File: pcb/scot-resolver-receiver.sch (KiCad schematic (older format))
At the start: 12 parts, among them IC3 AD8692ARMZ

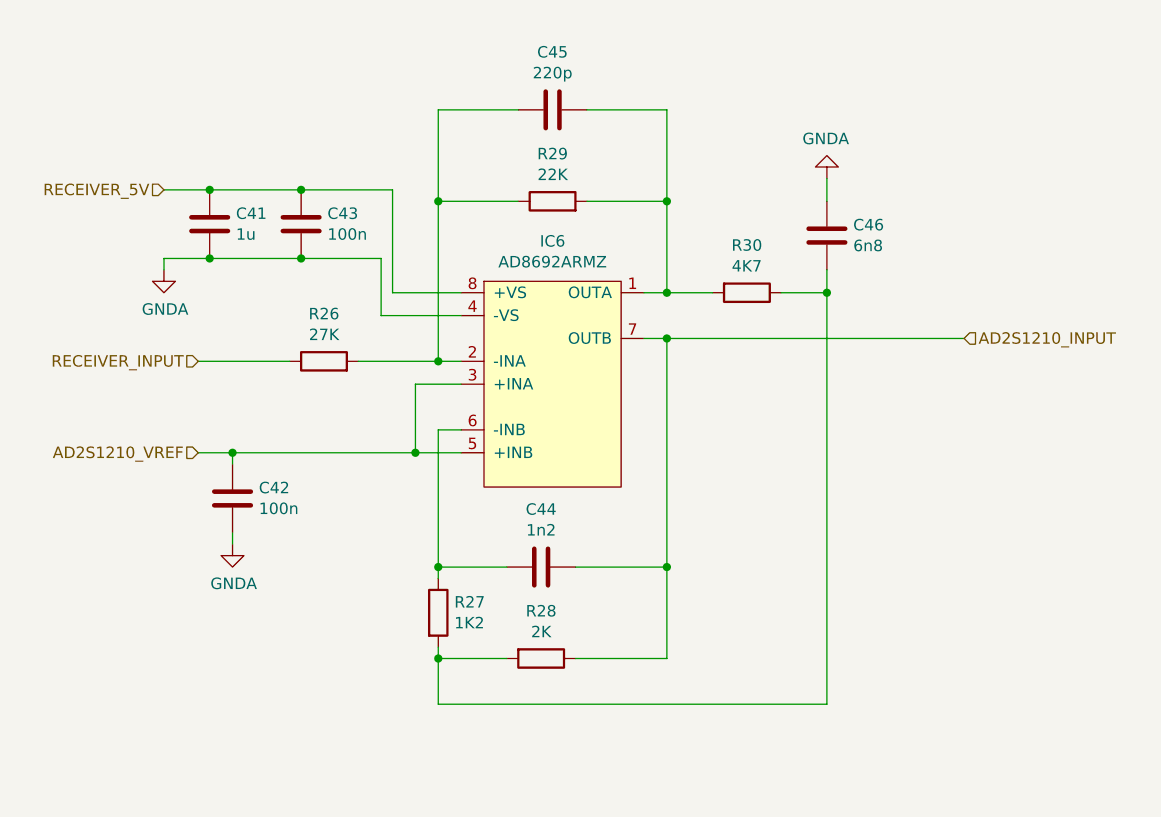
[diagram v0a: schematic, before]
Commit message: PCB Progress, laying tracks.
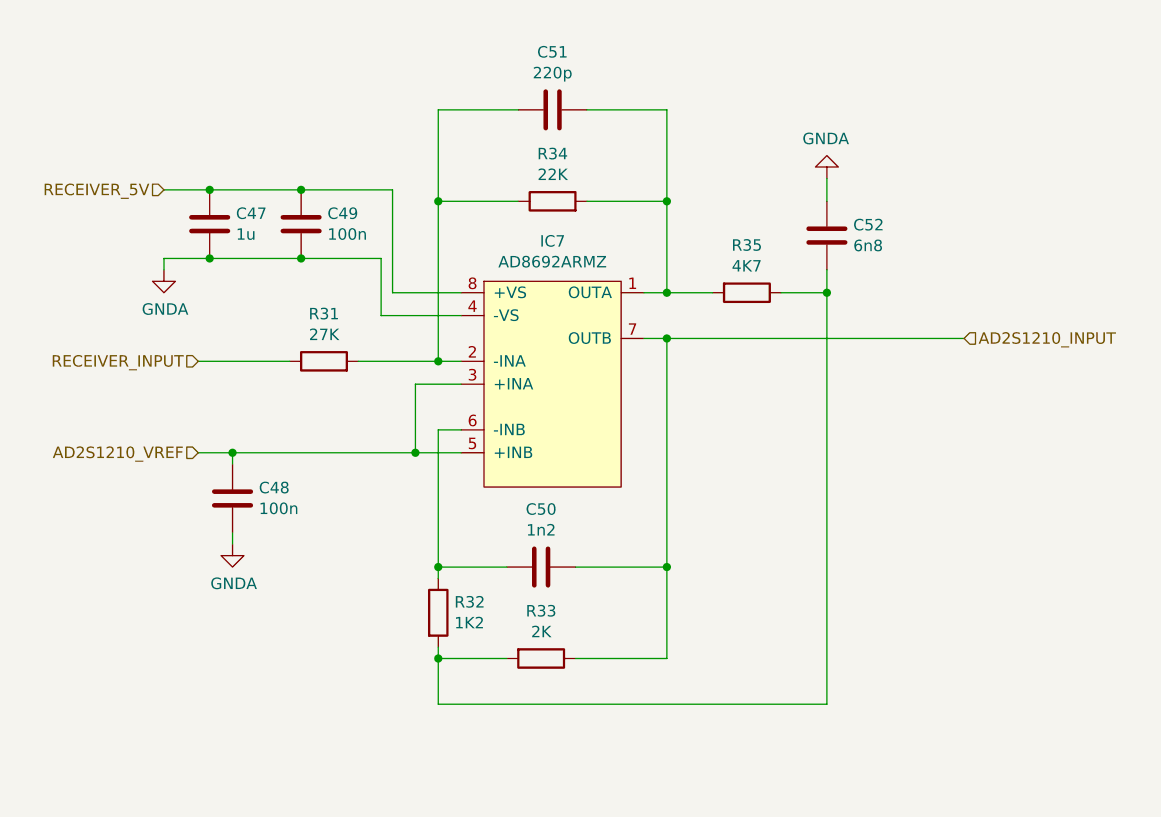
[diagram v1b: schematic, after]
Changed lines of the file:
@@
 $Descr A4 11693 8268
 encoding utf-8
-Sheet 6 9
+Sheet 7 9
 Title ""
 Date ""
@@
 AR Path="/5E46F57D/5E2564F7" Ref="IC6"  Part="1"
 AR Path="/5E46F583/5E2564F7" Ref="IC7"  Part="1"
-F 0 "IC6" H 5100 3925 50  0000 C CNN
+F 0 "IC7" H 5100 3925 50  0000 C CNN
 F 1 "AD8692ARMZ" H 5100 3834 50  0000 C CNN
 F 2 "agg:MSOP-8" H 4800 2700 50  0001 L CNN
@@
 AR Path="/5E46F57D/5E256D1D" Ref="R30"  Part="1"
 AR Path="/5E46F583/5E256D1D" Ref="R35"  Part="1"
-F 0 "R30" V 5743 2900 50  0000 C CNN
+F 0 "R35" V 5743 2900 50  0000 C CNN
 F 1 "4K7" V 5834 2900 50  0000 C CNN
 F 2 "Resistor_SMD:R_0402_1005Metric" V 5880 2900 50  0001 C CNN
@@
 AR Path="/5E46F57D/5E257610" Ref="C46"  Part="1"
 AR Path="/5E46F583/5E257610" Ref="C52"  Part="1"
-F 0 "C46" H 6185 2604 50  0000 R CNN
+F 0 "C52" H 6185 2604 50  0000 R CNN
 F 1 "6n8" H 6185 2695 50  0000 R CNN
 F 2 "Capacitor_SMD:C_0402_1005Metric" H 6338 2500 50  0001 C CNN
@@
 AR Path="/5E46F57D/5E258A95" Ref="R28"  Part="1"
 AR Path="/5E46F583/5E258A95" Ref="R33"  Part="1"
-F 0 "R28" V 4843 4500 50  0000 C CNN
+F 0 "R33" V 4843 4500 50  0000 C CNN
 F 1 "2K" V 4934 4500 50  0000 C CNN
 F 2 "Resistor_SMD:R_0402_1005Metric" V 4980 4500 50  0001 C CNN
@@
 AR Path="/5E46F57D/5E258E42" Ref="C44"  Part="1"
 AR Path="/5E46F583/5E258E42" Ref="C50"  Part="1"
-F 0 "C44" V 5302 4100 50  0000 C CNN
+F 0 "C50" V 5302 4100 50  0000 C CNN
 F 1 "1n2" V 5211 4100 50  0000 C CNN
 F 2 "Capacitor_SMD:C_0402_1005Metric" H 5088 3950 50  0001 C CNN
@@
 AR Path="/5E46F57D/5E25A0BD" Ref="R27"  Part="1"
 AR Path="/5E46F583/5E25A0BD" Ref="R32"  Part="1"
-F 0 "R27" H 4670 4346 50  0000 L CNN
+F 0 "R32" H 4670 4346 50  0000 L CNN
 F 1 "1K2" H 4670 4255 50  0000 L CNN
 F 2 "Resistor_SMD:R_0402_1005Metric" V 4530 4300 50  0001 C CNN
@@
 AR Path="/5E46F57D/5E25CCF3" Ref="R29"  Part="1"
 AR Path="/5E46F583/5E25CCF3" Ref="R34"  Part="1"
-F 0 "R29" V 5307 2500 50  0000 C CNN
+F 0 "R34" V 5307 2500 50  0000 C CNN
 F 1 "22K" V 5216 2500 50  0000 C CNN
 F 2 "Resistor_SMD:R_0402_1005Metric" V 5030 2500 50  0001 C CNN
@@
 AR Path="/5E46F57D/5E25ECB5" Ref="C45"  Part="1"
 AR Path="/5E46F583/5E25ECB5" Ref="C51"  Part="1"
-F 0 "C45" V 5352 2100 50  0000 C CNN
+F 0 "C51" V 5352 2100 50  0000 C CNN
 F 1 "220p" V 5261 2100 50  0000 C CNN
 F 2 "Capacitor_SMD:C_0402_1005Metric" H 5138 1950 50  0001 C CNN
@@
 AR Path="/5E46F57D/5E25FD02" Ref="R26"  Part="1"
 AR Path="/5E46F583/5E25FD02" Ref="R31"  Part="1"
-F 0 "R26" V 4307 3200 50  0000 C CNN
+F 0 "R31" V 4307 3200 50  0000 C CNN
 F 1 "27K" V 4216 3200 50  0000 C CNN
 F 2 "Resistor_SMD:R_0402_1005Metric" V 4030 3200 50  0001 C CNN
@@
 AR Path="/5E46F57D/5E281514" Ref="C43"  Part="1"
 AR Path="/5E46F583/5E281514" Ref="C49"  Part="1"
-F 0 "C43" H 3885 2554 50  0000 R CNN
+F 0 "C49" H 3885 2554 50  0000 R CNN
 F 1 "100n" H 3885 2645 50  0000 R CNN
 F 2 "Capacitor_SMD:C_0402_1005Metric" H 4038 2450 50  0001 C CNN
@@
 AR Path="/5E46F57D/5E297D03" Ref="C42"  Part="1"
 AR Path="/5E46F583/5E297D03" Ref="C48"  Part="1"
-F 0 "C42" H 3585 3754 50  0000 R CNN
+F 0 "C48" H 3585 3754 50  0000 R CNN
 F 1 "100n" H 3585 3845 50  0000 R CNN
 F 2 "Capacitor_SMD:C_0402_1005Metric" H 3738 3650 50  0001 C CNN
@@
 AR Path="/5E46F57D/5E29C4B1" Ref="C41"  Part="1"
 AR Path="/5E46F583/5E29C4B1" Ref="C47"  Part="1"
-F 0 "C41" H 3485 2554 50  0000 R CNN
+F 0 "C47" H 3485 2554 50  0000 R CNN
 F 1 "1u" H 3485 2645 50  0000 R CNN
 F 2 "Capacitor_SMD:C_0603_1608Metric_Pad1.05x0.95mm_HandSolder" H 3638 2450 50  0001 C CNN
@@
 AR Path="/5E46F57D/5E28F597" Ref="#PWR0130"  Part="1"
 AR Path="/5E46F583/5E28F597" Ref="#PWR0133"  Part="1"
-F 0 "#PWR0130" H 3400 2550 50  0001 C CNN
+F 0 "#PWR0133" H 3400 2550 50  0001 C CNN
 F 1 "GNDA" H 3405 2627 50  0000 C CNN
 F 2 "" H 3400 2800 50  0001 C CNN
@@
 AR Path="/5E46F57D/5E28F9AD" Ref="#PWR0131"  Part="1"
 AR Path="/5E46F583/5E28F9AD" Ref="#PWR0134"  Part="1"
-F 0 "#PWR0131" H 3700 3750 50  0001 C CNN
+F 0 "#PWR0134" H 3700 3750 50  0001 C CNN
 F 1 "GNDA" H 3705 3827 50  0000 C CNN
 F 2 "" H 3700 4000 50  0001 C CNN
@@
 AR Path="/5E46F57D/5E28FD4C" Ref="#PWR0132"  Part="1"
 AR Path="/5E46F583/5E28FD4C" Ref="#PWR0135"  Part="1"
-F 0 "#PWR0132" H 6300 2150 50  0001 C CNN
+F 0 "#PWR0135" H 6300 2150 50  0001 C CNN
 F 1 "GNDA" H 6305 2227 50  0000 C CNN
 F 2 "" H 6300 2400 50  0001 C CNN

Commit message: pcb: V2 schematic updates (PCB still to do).
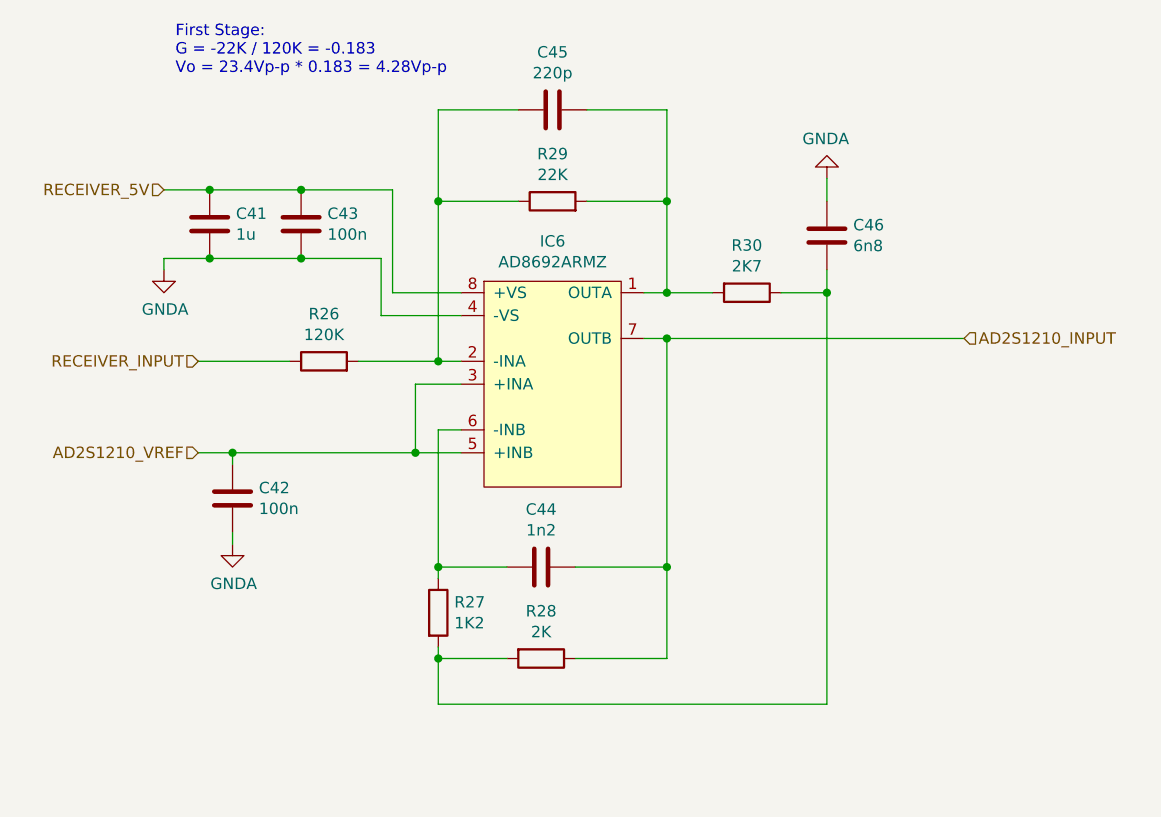
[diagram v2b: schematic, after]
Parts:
- R13: value 27K -> 120K
- R17: value 4K7 -> 2K7
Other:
- note added: "First Stage:\nG = -22K / 120K = -0.183\nVo = 23.4Vp-p * 0.183 = 4.28Vp-p"
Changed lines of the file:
@@
 $Descr A4 11693 8268
 encoding utf-8
-Sheet 7 9
+Sheet 5 7
 Title ""
 Date ""
@@
 AR Path="/5E46F57D/5E2564F7" Ref="IC6"  Part="1"
 AR Path="/5E46F583/5E2564F7" Ref="IC7"  Part="1"
-F 0 "IC7" H 5100 3925 50  0000 C CNN
+F 0 "IC6" H 5100 3925 50  0000 C CNN
 F 1 "AD8692ARMZ" H 5100 3834 50  0000 C CNN
 F 2 "agg:MSOP-8" H 4800 2700 50  0001 L CNN
@@
 AR Path="/5E46F57D/5E256D1D" Ref="R30"  Part="1"
 AR Path="/5E46F583/5E256D1D" Ref="R35"  Part="1"
-F 0 "R35" V 5743 2900 50  0000 C CNN
-F 1 "4K7" V 5834 2900 50  0000 C CNN
+F 0 "R30" V 5743 2900 50  0000 C CNN
+F 1 "2K7" V 5834 2900 50  0000 C CNN
 F 2 "Resistor_SMD:R_0402_1005Metric" V 5880 2900 50  0001 C CNN
 F 3 "~" H 5950 2900 50  0001 C CNN
@@
 AR Path="/5E46F57D/5E257610" Ref="C46"  Part="1"
 AR Path="/5E46F583/5E257610" Ref="C52"  Part="1"
-F 0 "C52" H 6185 2604 50  0000 R CNN
+F 0 "C46" H 6185 2604 50  0000 R CNN
 F 1 "6n8" H 6185 2695 50  0000 R CNN
 F 2 "Capacitor_SMD:C_0402_1005Metric" H 6338 2500 50  0001 C CNN
@@
 AR Path="/5E46F57D/5E258A95" Ref="R28"  Part="1"
 AR Path="/5E46F583/5E258A95" Ref="R33"  Part="1"
-F 0 "R33" V 4843 4500 50  0000 C CNN
+F 0 "R28" V 4843 4500 50  0000 C CNN
 F 1 "2K" V 4934 4500 50  0000 C CNN
 F 2 "Resistor_SMD:R_0402_1005Metric" V 4980 4500 50  0001 C CNN
@@
 AR Path="/5E46F57D/5E258E42" Ref="C44"  Part="1"
 AR Path="/5E46F583/5E258E42" Ref="C50"  Part="1"
-F 0 "C50" V 5302 4100 50  0000 C CNN
+F 0 "C44" V 5302 4100 50  0000 C CNN
 F 1 "1n2" V 5211 4100 50  0000 C CNN
 F 2 "Capacitor_SMD:C_0402_1005Metric" H 5088 3950 50  0001 C CNN
@@
 AR Path="/5E46F57D/5E25A0BD" Ref="R27"  Part="1"
 AR Path="/5E46F583/5E25A0BD" Ref="R32"  Part="1"
-F 0 "R32" H 4670 4346 50  0000 L CNN
+F 0 "R27" H 4670 4346 50  0000 L CNN
 F 1 "1K2" H 4670 4255 50  0000 L CNN
 F 2 "Resistor_SMD:R_0402_1005Metric" V 4530 4300 50  0001 C CNN
@@
 AR Path="/5E46F57D/5E25CCF3" Ref="R29"  Part="1"
 AR Path="/5E46F583/5E25CCF3" Ref="R34"  Part="1"
-F 0 "R34" V 5307 2500 50  0000 C CNN
+F 0 "R29" V 5307 2500 50  0000 C CNN
 F 1 "22K" V 5216 2500 50  0000 C CNN
 F 2 "Resistor_SMD:R_0402_1005Metric" V 5030 2500 50  0001 C CNN
@@
 AR Path="/5E46F57D/5E25ECB5" Ref="C45"  Part="1"
 AR Path="/5E46F583/5E25ECB5" Ref="C51"  Part="1"
-F 0 "C51" V 5352 2100 50  0000 C CNN
+F 0 "C45" V 5352 2100 50  0000 C CNN
 F 1 "220p" V 5261 2100 50  0000 C CNN
 F 2 "Capacitor_SMD:C_0402_1005Metric" H 5138 1950 50  0001 C CNN
@@
 AR Path="/5E46F57D/5E25FD02" Ref="R26"  Part="1"
 AR Path="/5E46F583/5E25FD02" Ref="R31"  Part="1"
-F 0 "R31" V 4307 3200 50  0000 C CNN
-F 1 "27K" V 4216 3200 50  0000 C CNN
+F 0 "R26" V 4307 3200 50  0000 C CNN
+F 1 "120K" V 4216 3200 50  0000 C CNN
 F 2 "Resistor_SMD:R_0402_1005Metric" V 4030 3200 50  0001 C CNN
 F 3 "~" H 4100 3200 50  0001 C CNN
@@
 AR Path="/5E46F57D/5E281514" Ref="C43"  Part="1"
 AR Path="/5E46F583/5E281514" Ref="C49"  Part="1"
-F 0 "C49" H 3885 2554 50  0000 R CNN
+F 0 "C43" H 3885 2554 50  0000 R CNN
 F 1 "100n" H 3885 2645 50  0000 R CNN
 F 2 "Capacitor_SMD:C_0402_1005Metric" H 4038 2450 50  0001 C CNN
@@
 AR Path="/5E46F57D/5E297D03" Ref="C42"  Part="1"
 AR Path="/5E46F583/5E297D03" Ref="C48"  Part="1"
-F 0 "C48" H 3585 3754 50  0000 R CNN
+F 0 "C42" H 3585 3754 50  0000 R CNN
 F 1 "100n" H 3585 3845 50  0000 R CNN
 F 2 "Capacitor_SMD:C_0402_1005Metric" H 3738 3650 50  0001 C CNN
@@
 AR Path="/5E46F57D/5E29C4B1" Ref="C41"  Part="1"
 AR Path="/5E46F583/5E29C4B1" Ref="C47"  Part="1"
-F 0 "C47" H 3485 2554 50  0000 R CNN
+F 0 "C41" H 3485 2554 50  0000 R CNN
 F 1 "1u" H 3485 2645 50  0000 R CNN
 F 2 "Capacitor_SMD:C_0603_1608Metric_Pad1.05x0.95mm_HandSolder" H 3638 2450 50  0001 C CNN
@@
 AR Path="/5E46F57D/5E28F597" Ref="#PWR0130"  Part="1"
 AR Path="/5E46F583/5E28F597" Ref="#PWR0133"  Part="1"
-F 0 "#PWR0133" H 3400 2550 50  0001 C CNN
+F 0 "#PWR0130" H 3400 2550 50  0001 C CNN
 F 1 "GNDA" H 3405 2627 50  0000 C CNN
 F 2 "" H 3400 2800 50  0001 C CNN
@@
 AR Path="/5E46F57D/5E28F9AD" Ref="#PWR0131"  Part="1"
 AR Path="/5E46F583/5E28F9AD" Ref="#PWR0134"  Part="1"
-F 0 "#PWR0134" H 3700 3750 50  0001 C CNN
+F 0 "#PWR0131" H 3700 3750 50  0001 C CNN
 F 1 "GNDA" H 3705 3827 50  0000 C CNN
 F 2 "" H 3700 4000 50  0001 C CNN
@@
 AR Path="/5E46F57D/5E28FD4C" Ref="#PWR0132"  Part="1"
 AR Path="/5E46F583/5E28FD4C" Ref="#PWR0135"  Part="1"
-F 0 "#PWR0135" H 6300 2150 50  0001 C CNN
+F 0 "#PWR0132" H 6300 2150 50  0001 C CNN
 F 1 "GNDA" H 6305 2227 50  0000 C CNN
 F 2 "" H 6300 2400 50  0001 C CNN
@@
 	-1   0    0    1
 $EndComp
+Text Notes 3450 1950 0    50   ~ 0
+First Stage:\nG = -22K / 120K = -0.183\nVo = 23.4Vp-p * 0.183 = 4.28Vp-p
 $EndSCHEMATC

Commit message: pcb: Add Receiver second stage calculations to schematic.
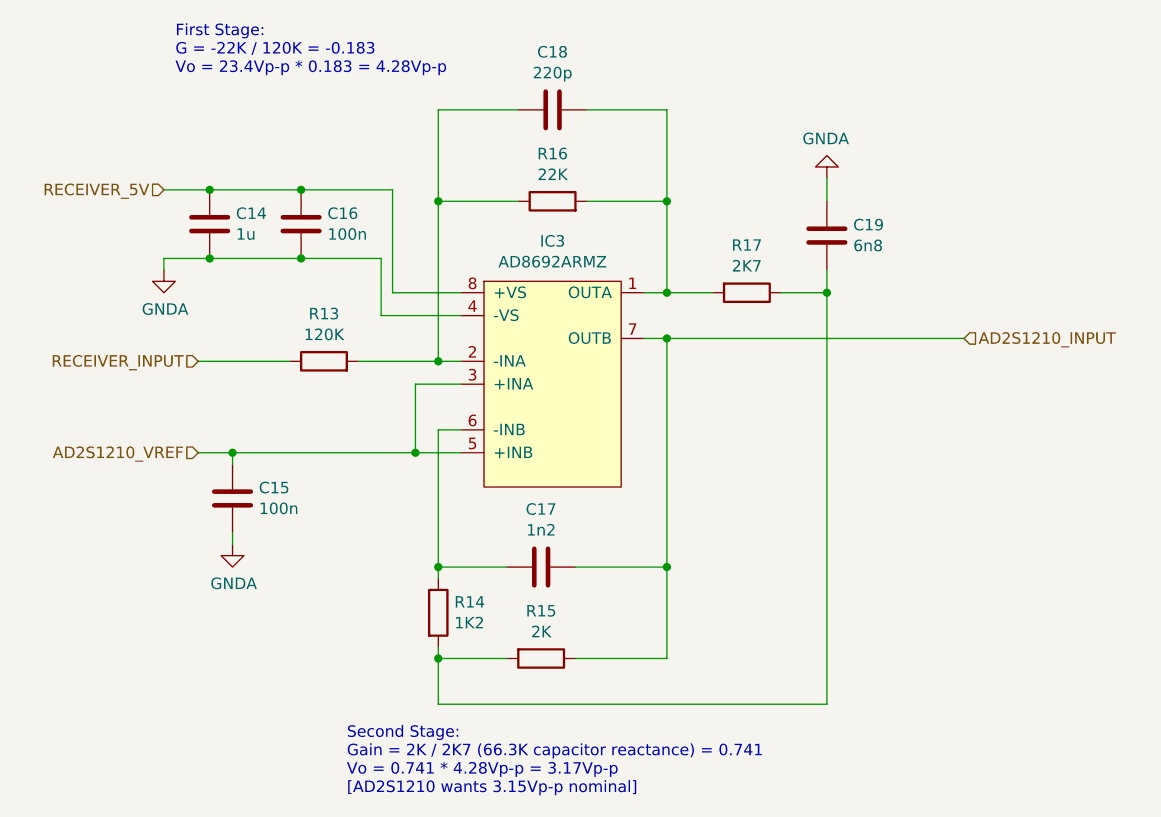
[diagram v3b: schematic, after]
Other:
- note added: "Second Stage:\nGain = 2K / 2K7 (66.3K capacitor reactance) = 0.741\nVo = 0.741 * 4.28Vp-p = 3.17Vp-p\n[AD2S1210 wants 3.15Vp-p nominal]"
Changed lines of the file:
@@
 $Descr A4 11693 8268
 encoding utf-8
-Sheet 5 7
+Sheet 3 7
 Title ""
 Date ""
@@
 AR Path="/5E46F57D/5E2564F7" Ref="IC6"  Part="1"
 AR Path="/5E46F583/5E2564F7" Ref="IC7"  Part="1"
-F 0 "IC6" H 5100 3925 50  0000 C CNN
+F 0 "IC3" H 5100 3925 50  0000 C CNN
 F 1 "AD8692ARMZ" H 5100 3834 50  0000 C CNN
 F 2 "agg:MSOP-8" H 4800 2700 50  0001 L CNN
@@
 AR Path="/5E46F57D/5E256D1D" Ref="R30"  Part="1"
 AR Path="/5E46F583/5E256D1D" Ref="R35"  Part="1"
-F 0 "R30" V 5743 2900 50  0000 C CNN
+F 0 "R17" V 5743 2900 50  0000 C CNN
 F 1 "2K7" V 5834 2900 50  0000 C CNN
 F 2 "Resistor_SMD:R_0402_1005Metric" V 5880 2900 50  0001 C CNN
@@
 AR Path="/5E46F57D/5E257610" Ref="C46"  Part="1"
 AR Path="/5E46F583/5E257610" Ref="C52"  Part="1"
-F 0 "C46" H 6185 2604 50  0000 R CNN
+F 0 "C19" H 6185 2604 50  0000 R CNN
 F 1 "6n8" H 6185 2695 50  0000 R CNN
 F 2 "Capacitor_SMD:C_0402_1005Metric" H 6338 2500 50  0001 C CNN
@@
 AR Path="/5E46F57D/5E258A95" Ref="R28"  Part="1"
 AR Path="/5E46F583/5E258A95" Ref="R33"  Part="1"
-F 0 "R28" V 4843 4500 50  0000 C CNN
+F 0 "R15" V 4843 4500 50  0000 C CNN
 F 1 "2K" V 4934 4500 50  0000 C CNN
 F 2 "Resistor_SMD:R_0402_1005Metric" V 4980 4500 50  0001 C CNN
@@
 AR Path="/5E46F57D/5E258E42" Ref="C44"  Part="1"
 AR Path="/5E46F583/5E258E42" Ref="C50"  Part="1"
-F 0 "C44" V 5302 4100 50  0000 C CNN
+F 0 "C17" V 5302 4100 50  0000 C CNN
 F 1 "1n2" V 5211 4100 50  0000 C CNN
 F 2 "Capacitor_SMD:C_0402_1005Metric" H 5088 3950 50  0001 C CNN
@@
 AR Path="/5E46F57D/5E25A0BD" Ref="R27"  Part="1"
 AR Path="/5E46F583/5E25A0BD" Ref="R32"  Part="1"
-F 0 "R27" H 4670 4346 50  0000 L CNN
+F 0 "R14" H 4670 4346 50  0000 L CNN
 F 1 "1K2" H 4670 4255 50  0000 L CNN
 F 2 "Resistor_SMD:R_0402_1005Metric" V 4530 4300 50  0001 C CNN
@@
 AR Path="/5E46F57D/5E25CCF3" Ref="R29"  Part="1"
 AR Path="/5E46F583/5E25CCF3" Ref="R34"  Part="1"
-F 0 "R29" V 5307 2500 50  0000 C CNN
+F 0 "R16" V 5307 2500 50  0000 C CNN
 F 1 "22K" V 5216 2500 50  0000 C CNN
 F 2 "Resistor_SMD:R_0402_1005Metric" V 5030 2500 50  0001 C CNN
@@
 AR Path="/5E46F57D/5E25ECB5" Ref="C45"  Part="1"
 AR Path="/5E46F583/5E25ECB5" Ref="C51"  Part="1"
-F 0 "C45" V 5352 2100 50  0000 C CNN
+F 0 "C18" V 5352 2100 50  0000 C CNN
 F 1 "220p" V 5261 2100 50  0000 C CNN
 F 2 "Capacitor_SMD:C_0402_1005Metric" H 5138 1950 50  0001 C CNN
@@
 AR Path="/5E46F57D/5E25FD02" Ref="R26"  Part="1"
 AR Path="/5E46F583/5E25FD02" Ref="R31"  Part="1"
-F 0 "R26" V 4307 3200 50  0000 C CNN
+F 0 "R13" V 4307 3200 50  0000 C CNN
 F 1 "120K" V 4216 3200 50  0000 C CNN
 F 2 "Resistor_SMD:R_0402_1005Metric" V 4030 3200 50  0001 C CNN
@@
 AR Path="/5E46F57D/5E281514" Ref="C43"  Part="1"
 AR Path="/5E46F583/5E281514" Ref="C49"  Part="1"
-F 0 "C43" H 3885 2554 50  0000 R CNN
+F 0 "C16" H 3885 2554 50  0000 R CNN
 F 1 "100n" H 3885 2645 50  0000 R CNN
 F 2 "Capacitor_SMD:C_0402_1005Metric" H 4038 2450 50  0001 C CNN
@@
 AR Path="/5E46F57D/5E297D03" Ref="C42"  Part="1"
 AR Path="/5E46F583/5E297D03" Ref="C48"  Part="1"
-F 0 "C42" H 3585 3754 50  0000 R CNN
+F 0 "C15" H 3585 3754 50  0000 R CNN
 F 1 "100n" H 3585 3845 50  0000 R CNN
 F 2 "Capacitor_SMD:C_0402_1005Metric" H 3738 3650 50  0001 C CNN
@@
 AR Path="/5E46F57D/5E29C4B1" Ref="C41"  Part="1"
 AR Path="/5E46F583/5E29C4B1" Ref="C47"  Part="1"
-F 0 "C41" H 3485 2554 50  0000 R CNN
+F 0 "C14" H 3485 2554 50  0000 R CNN
 F 1 "1u" H 3485 2645 50  0000 R CNN
 F 2 "Capacitor_SMD:C_0603_1608Metric_Pad1.05x0.95mm_HandSolder" H 3638 2450 50  0001 C CNN
@@
 AR Path="/5E46F57D/5E28F597" Ref="#PWR0130"  Part="1"
 AR Path="/5E46F583/5E28F597" Ref="#PWR0133"  Part="1"
-F 0 "#PWR0130" H 3400 2550 50  0001 C CNN
+F 0 "#PWR0110" H 3400 2550 50  0001 C CNN
 F 1 "GNDA" H 3405 2627 50  0000 C CNN
 F 2 "" H 3400 2800 50  0001 C CNN
@@
 AR Path="/5E46F57D/5E28F9AD" Ref="#PWR0131"  Part="1"
 AR Path="/5E46F583/5E28F9AD" Ref="#PWR0134"  Part="1"
-F 0 "#PWR0131" H 3700 3750 50  0001 C CNN
+F 0 "#PWR0111" H 3700 3750 50  0001 C CNN
 F 1 "GNDA" H 3705 3827 50  0000 C CNN
 F 2 "" H 3700 4000 50  0001 C CNN
@@
 AR Path="/5E46F57D/5E28FD4C" Ref="#PWR0132"  Part="1"
 AR Path="/5E46F583/5E28FD4C" Ref="#PWR0135"  Part="1"
-F 0 "#PWR0132" H 6300 2150 50  0001 C CNN
+F 0 "#PWR0112" H 6300 2150 50  0001 C CNN
 F 1 "GNDA" H 6305 2227 50  0000 C CNN
 F 2 "" H 6300 2400 50  0001 C CNN
@@
 Text Notes 3450 1950 0    50   ~ 0
 First Stage:\nG = -22K / 120K = -0.183\nVo = 23.4Vp-p * 0.183 = 4.28Vp-p
+Text Notes 4200 5100 0    50   ~ 0
+Second Stage:\nGain = 2K / 2K7 (66.3K capacitor reactance) = 0.741\nVo = 0.741 * 4.28Vp-p = 3.17Vp-p\n[AD2S1210 wants 3.15Vp-p nominal]
 $EndSCHEMATC
